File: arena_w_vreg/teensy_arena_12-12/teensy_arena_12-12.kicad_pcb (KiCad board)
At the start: 4 copper layers, 254 x 254 mm, 87 parts, among them J1 Barrel_Jack, J2 Conn_01x04, J3 Conn_01x04, P1 CONN15, P10 CONN15, P11 CONN15, P12 CONN15, P2 CONN15, P3 CONN15, P4 CONN15, P5 CONN15, P6 CONN15, P7 CONN15, P8 CONN15, P9 CONN15, Q2 MOSFET_NCHAN, SW1 SW_SPDT, U1 TXB0108PW, U10 AZ1084-5.0, U11 AZ1084-5.0, U12 AZ1084-5.0, U13 AZ1084-5.0, U14 AZ1084-5.0, U15 AZ1084-5.0, U16 AZ1084-5.0, U17 AZ1084-5.0, U18 Teensy4.1, U2 TXB0108PW, U3 TXB0108PW, U4 TXB0108PW, U5 TXB0108PW, U6 AZ1084-5.0, U7 AZ1084-5.0, U8 AZ1084-5.0, U9 AZ1084-5.0

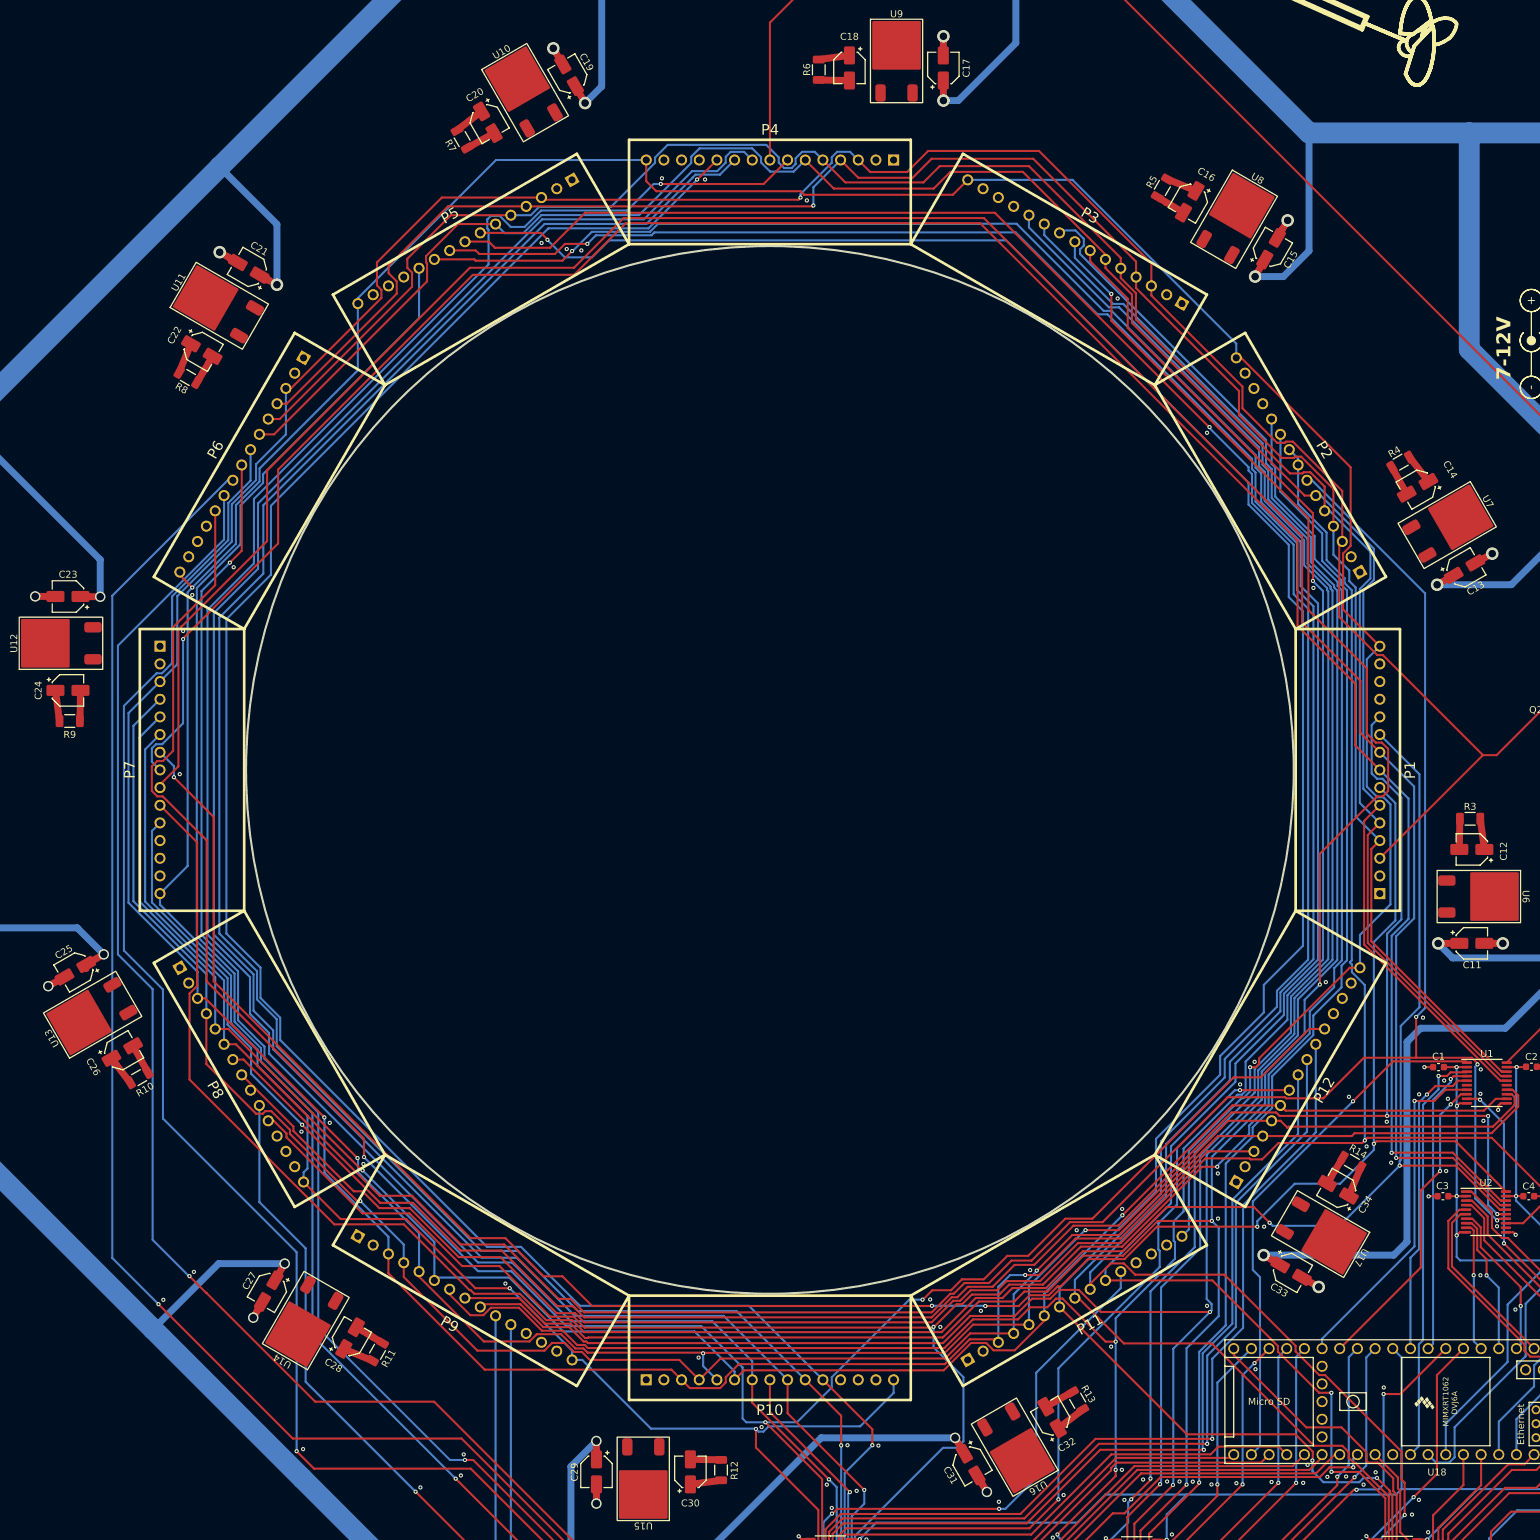
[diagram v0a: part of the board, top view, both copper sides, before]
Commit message: Finished initial version of fab files for 12-12 teensy controller arena.
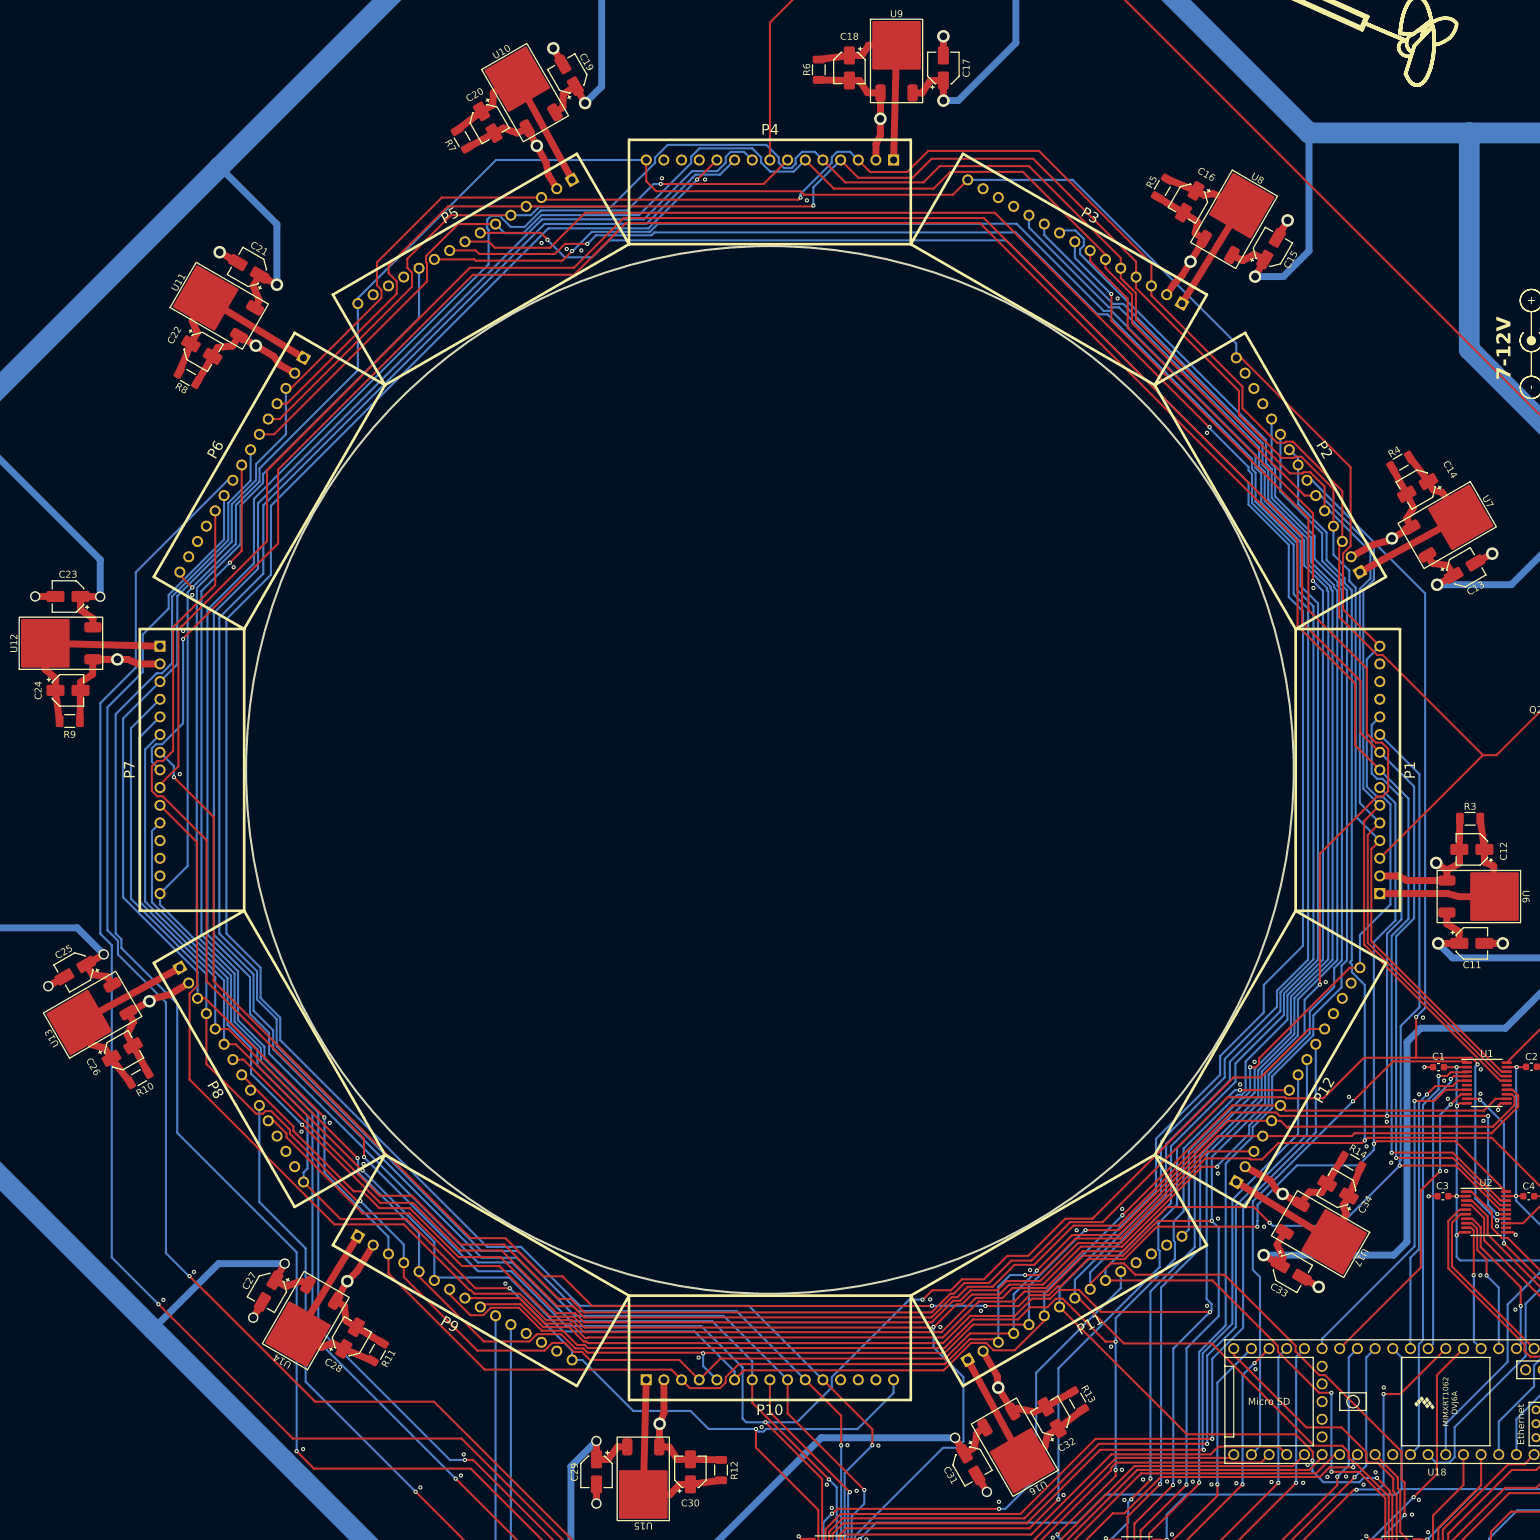
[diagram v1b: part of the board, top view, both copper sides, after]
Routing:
- net GND: track 135.5 -> 319.3 mm, vias 126 -> 138
- net VCC: track 1020.9 -> 1084.1 mm
- net /Panel Headers/POW.5V_HDR_1: track 4.44 -> 28.7 mm
- net /Panel Headers/POW.5V_HDR_5: track 4.44 -> 28.5 mm
- net /Panel Headers/POW.5V_HDR_4: track 4.44 -> 28.5 mm
- net /Panel Headers/POW.5V_HDR_6: track 4.44 -> 28.5 mm
- net /Panel Headers/POW.5V_HDR_7: track 4.44 -> 28.4 mm
- net /Panel Headers/POW.5V_HDR_9: track 4.44 -> 28.4 mm
- net /Panel Headers/POW.5V_HDR_10: track 4.44 -> 28.4 mm
- net /Panel Headers/POW.5V_HDR_8: track 5.60 -> 29.5 mm
- net /Panel Headers/POW.5V_HDR_11: track 4.44 -> 28.3 mm
- net /Panel Headers/POW.5V_HDR_12: track 4.64 -> 28.4 mm
- net /Panel Headers/POW.5V_HDR_2: track 4.44 -> 28.1 mm
- net /Panel Headers/POW.5V_HDR_3: track 4.44 -> 28.1 mm
- net /Level Shifters/PAN5V.CS_27: track 364.6 -> 366.0 mm
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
